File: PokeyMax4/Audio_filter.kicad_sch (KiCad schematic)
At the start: 8 parts, among them CN1 18nF, U1 TSV854IQ4T

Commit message: Update the v4 board
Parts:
- C3, C4: JLCPCB Part # C452745 -> (none); LCSC Part # (none) -> C12530
- CN1: JLCPCB Part # C3681031 -> (none); LCSC Part # (none) -> C3681031
- RN1: JLCPCB Part # C507417 -> (none); LCSC Part # (none) -> C507417
- RN2: JLCPCB Part # C2654027 -> (none); LCSC Part # (none) -> C2654027
- RN3: JLCPCB Part # C727854 -> (none); LCSC Part # (none) -> C727854
- U1: JLCPCB Part # C2058240 -> (none); LCSC Part # (none) -> C2058240

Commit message: Updates for JLCPCB fabrication and parts library
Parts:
- removed CN1: 18nF, pokeymax4:R1206-8, symbol pokeymax4-eagle-import:R-4R
- removed RN1: 20K, pokeymax4:741-8, symbol pokeymax4-eagle-import:741-8
- removed RN2: 10K, pokeymax4:741-8, symbol pokeymax4-eagle-import:741-8
- removed RN3: 560, pokeymax4:741-8, symbol pokeymax4-eagle-import:741-8
- added C13, C14, C15: 18nF, pokeymax4:C0402, symbol Device:C
- added R11, R12, R13: 560R, Resistor_SMD:R_0402_1005Metric, symbol Device:R
- added R14, R15, R16: 10k, Resistor_SMD:R_0402_1005Metric, symbol Device:R
- added R17, R18, R19: 20k, Resistor_SMD:R_0402_1005Metric, symbol Device:R
- AUD0: now left out of the parts list
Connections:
- net AUD1: now also R13.1
- net AUD3: now also R11.1
- net AUD4: now also R12.1
- net AUDF1: now also R14.1
- net GND: now also C13.2, C14.2, C15.2, R17.2, R18.2, R19.2
- net at U1.16 (IN1-): now also R14.2, R17.1
- net at U1.8 (IN3-): now also R15.2, R18.1
- net at U1.13 (IN4-): now also R16.2, R19.1
- net at C3.1, U1.14 (OUT4): now also R16.1
- net at C4.1, U1.7 (OUT3): now also R15.1
- net at U1.1 (IN1+): now also C15.1, R13.2
- net at U1.12 (IN4+): now also C14.1, R12.2
- net at U1.9 (IN3+): now also C13.1, R11.2

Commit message: Final adjustements to production files for JLC
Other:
- moved on the sheet: C3
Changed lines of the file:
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@@
+	(wire
+		(pts
+			(xy 185.42 104.14) (xy 185.42 101.6)
+		)
+		(stroke
+			(width 0.1524)
+			(type solid)
+		)
+	)
 	(wire
 		(pts
@@
 	(wire
 		(pts
-			(xy 185.42 101.6) (xy 203.2 101.6)
+			(xy 185.42 104.14) (xy 203.2 104.14)
 		)
 		(stroke
@@
 	(wire
 		(pts
-			(xy 226.06 104.14) (xy 215.9 104.14)
-		)
-		(stroke
-			(width 0.1524)
-			(type solid)
-		)
-	)
-	(wire
-		(pts
 			(xy 68.58 99.06) (xy 68.58 109.22)
 		)
@@
 	(wire
 		(pts
-			(xy 180.34 88.9) (xy 187.96 88.9)
-		)
-		(stroke
-			(width 0.1524)
-			(type solid)
-		)
-	)
-	(wire
-		(pts
 			(xy 132.08 152.4) (xy 111.76 152.4)
 		)
@@
 	(wire
 		(pts
-			(xy 215.9 101.6) (xy 210.82 101.6)
+			(xy 210.82 104.14) (xy 226.06 104.14)
 		)
 		(stroke
@@
 	(wire
 		(pts
-			(xy 187.96 86.36) (xy 180.34 86.36)
-		)
-		(stroke
-			(width 0.1524)
-			(type solid)
-		)
-	)
-	(wire
-		(pts
 			(xy 101.6 142.24) (xy 132.08 142.24)
 		)
@@
 	(wire
 		(pts
-			(xy 215.9 104.14) (xy 215.9 101.6)
-		)
-		(stroke
-			(width 0.1524)
-			(type solid)
-		)
-	)
-	(wire
-		(pts
 			(xy 190.5 99.06) (xy 190.5 58.42)
 		)
@@
 	)
 	(label "AUDF4"
-		(at 213.36 101.6 0)
+		(at 213.36 104.14 0)
 		(fields_autoplaced yes)
 		(effects
@@
 	(global_label "5V0"
 		(shape bidirectional)
-		(at 187.96 86.36 0)
+		(at 180.34 86.36 0)
 		(fields_autoplaced yes)
 		(effects
@@
 		)
 		(property "Intersheetrefs" "${INTERSHEET_REFS}"
-			(at 195.4116 86.36 0)
+			(at 187.7916 86.36 0)
 			(effects
 				(font
@@
 	(global_label "GND"
 		(shape bidirectional)
-		(at 187.96 88.9 0)
+		(at 180.34 88.9 0)
 		(fields_autoplaced yes)
 		(effects
@@
 		)
 		(property "Intersheetrefs" "${INTERSHEET_REFS}"
-			(at 195.7673 88.9 0)
+			(at 188.1473 88.9 0)
 			(effects
 				(font
@@
 	(global_label "AUDF1"
 		(shape bidirectional)
-		(at 187.96 93.98 0)
+		(at 195.58 53.34 0)
 		(fields_autoplaced yes)
 		(effects
@@
 		)
 		(property "Intersheetrefs" "${INTERSHEET_REFS}"
-			(at 197.8416 93.98 0)
+			(at 205.4616 53.34 0)
 			(effects
 				(font
@@
 	(symbol
 		(lib_id "pokeymax4-eagle-import:C-EUC0402")
-		(at 205.74 101.6 90)
+		(at 205.74 104.14 90)
 		(unit 1)
 		(exclude_from_sim no)
@@
 		(dnp no)
 		(property "Reference" "C3"
-			(at 205.359 100.076 0)
+			(at 205.486 108.204 0)
 			(effects
 				(font
@@
 		)
 		(property "Value" "2.2uF"
-			(at 210.439 100.076 0)
+			(at 210.82 111.506 0)
 			(effects
 				(font
@@
 		)
 		(property "Footprint" "pokeymax4:C0402"
-			(at 205.74 101.6 0)
+			(at 205.74 104.14 0)
 			(effects
 				(font
@@
 		)
 		(property "Datasheet" ""
-			(at 205.74 101.6 0)
+			(at 205.74 104.14 0)
 			(effects
 				(font
@@
 		)
 		(property "Description" ""
-			(at 205.74 101.6 0)
+			(at 205.74 104.14 0)
 			(effects
 				(font
@@
 		)
 		(property "LCSC Part #" "C12530"
-			(at 205.74 101.6 0)
+			(at 205.74 104.14 0)
 			(effects
 				(font
@@
 		)
 		(property "JLCPCB Rotation Offset" ""
-			(at 205.74 101.6 0)
-			(effects
-				(font
+			(at 205.74 104.14 0)
+			(effects
+				(font

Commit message: Update BOM from 0402 to 0603 where relevant
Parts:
- C13, C14, C15: LCSC Part # C107016 -> C107079
- C3, C4: LCSC Part # C12530 -> C43922
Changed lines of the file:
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@@
 			)
 		)
-		(property "LCSC Part #" "C107016"
+		(property "LCSC Part #" "C107079"
 			(at 135.89 142.24 0)
 			(effects
@@
 			)
 		)
-		(property "LCSC Part #" "C107016"
+		(property "LCSC Part #" "C107079"
 			(at 135.89 147.32 0)
 			(effects
@@
 			)
 		)
-		(property "LCSC Part #" "C12530"
+		(property "LCSC Part #" "C43922"
 			(at 205.74 104.14 0)
 			(effects
@@
 			)
 		)
-		(property "LCSC Part #" "C107016"
+		(property "LCSC Part #" "C107079"
 			(at 135.89 152.4 0)
 			(effects
@@
 			)
 		)
-		(property "LCSC Part #" "C12530"
+		(property "LCSC Part #" "C43922"
 			(at 205.74 99.06 0)
 			(effects

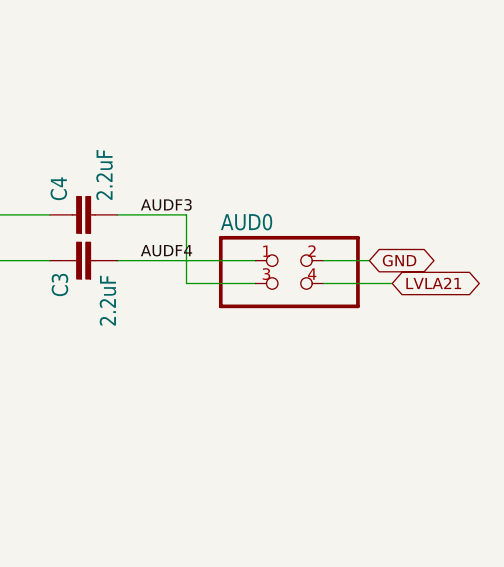
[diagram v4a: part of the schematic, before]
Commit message: Add A4 to PokeyMax 4s
Reroute accordingly
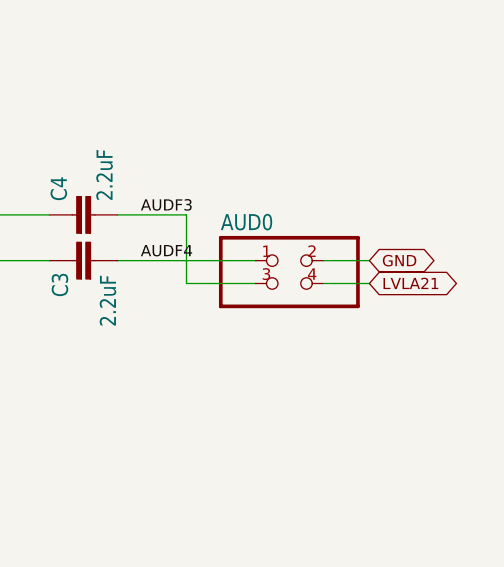
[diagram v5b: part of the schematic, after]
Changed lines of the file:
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@@
 	(wire
 		(pts
-			(xy 233.68 106.68) (xy 241.3 106.68)
+			(xy 233.68 106.68) (xy 238.76 106.68)
 		)
 		(stroke
@@
 	(global_label "LVLA21"
 		(shape bidirectional)
-		(at 241.3 106.68 0)
+		(at 238.76 106.68 0)
 		(fields_autoplaced yes)
 		(effects
@@
 		)
 		(property "Intersheetrefs" "${INTERSHEET_REFS}"
-			(at 251.8334 106.68 0)
+			(at 249.2934 106.68 0)
 			(effects
 				(font
